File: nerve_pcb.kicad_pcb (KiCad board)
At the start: 6 copper layers, 50 x 50 mm, 72 parts, among them J1 TC2050-IDC, J2 2171750001, J4 472192001, J5 BF030-16A-B1-0360-0277-0600-LB, J6 2x15, J7 CAN1, J8 CAN2, SW1 SPST, SW2 SPST, U1 ld39150dt33-r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

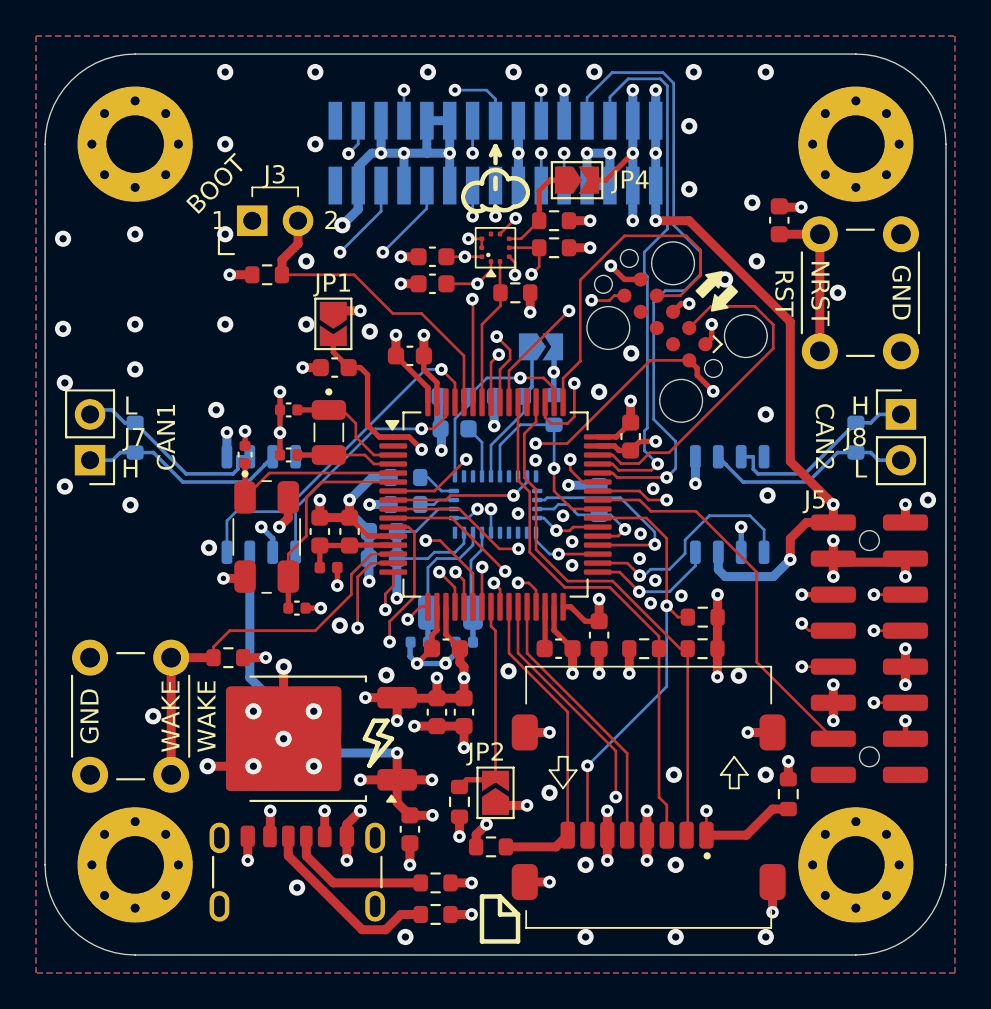
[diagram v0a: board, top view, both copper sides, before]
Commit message: Cleanup and update 2x10 Radio connector
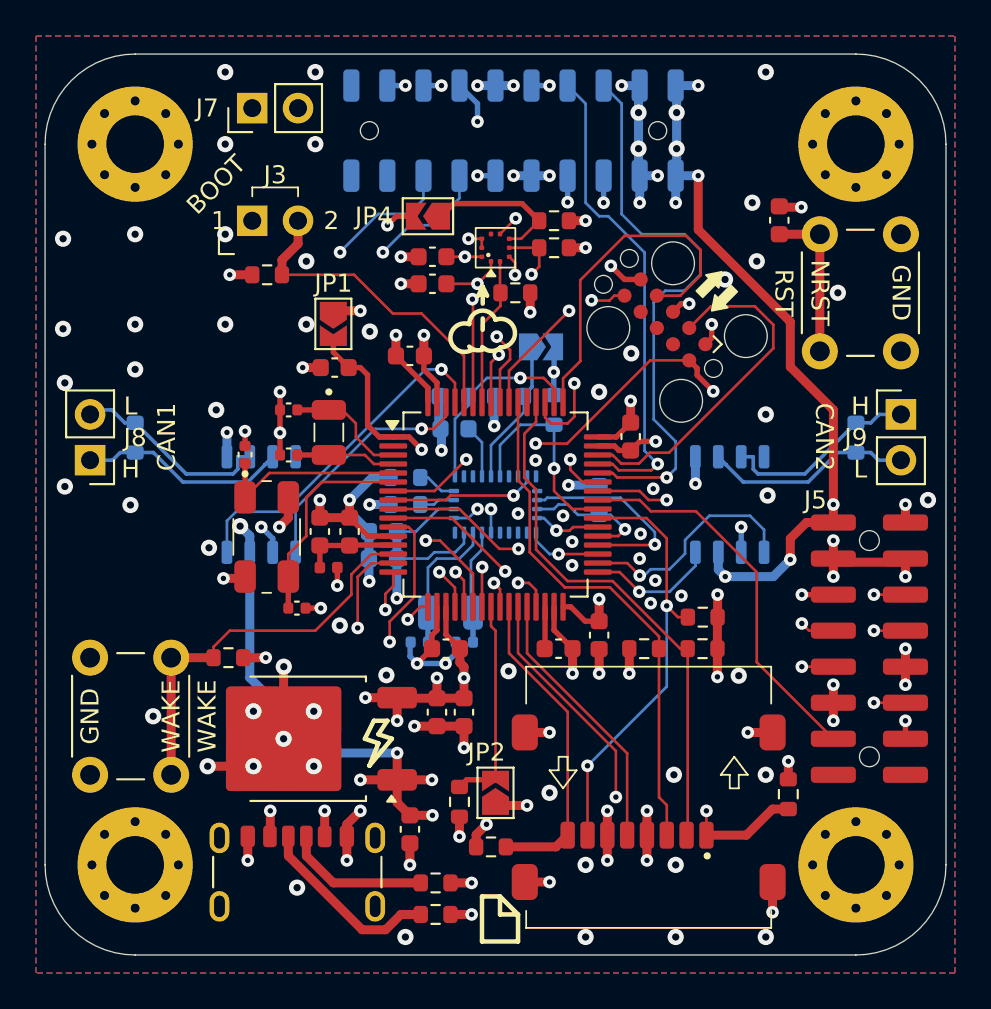
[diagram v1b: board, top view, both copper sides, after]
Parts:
- added J7: UART, Connector_PinHeader_2.54mm:PinHeader_1x02_P2.54mm_Vertical, F.Cu at (135.0, 83.0)
- J6: value 2x15 -> BF080-20-A-1-L-C; footprint Connector_PinSocket_1.27mm:PinSocket_2x15_P1.27mm_Vertical_SMD -> connectors:bf080-20-a-1-l-c
- moved JP4 8.51 mm to (144.8, 89.0), turned to 180 degrees
- moved J6 1.60 mm to (149.5, 84.2), turned to 180 degrees
- renumbered J7 to J8, J8 to J9
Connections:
- J6 pad 10: /USART1_TX -> GND
- J6 pad 11: /GPIO_RADIO_RST -> GND
- J6 pad 12: /USART1_RX -> /PB5
- J6 pad 13: GND -> /PB4
- J6 pad 14: GND -> /PA6
- J6 pad 15: /PA4 -> /PA5
- J6 pad 16: /PB4 -> /PA7
- J6 pad 17: /PA5 -> /PA4
- J6 pad 18: /PB5 -> GND
- J6 pad 19: GND -> unconnected-(J6-Pad19)
- J6 pad 20: GND -> unconnected-(J6-Pad20)
- J6 pad 5: /USART1_RTS -> /USART1_CTS
- J6 pad 6: GND -> /USART1_TX
- J6 pad 7: /USART1_CTS -> /USART1_RTS
- J6 pad 8: GND -> /USART1_RX
- J6 pad 9: GND -> /GPIO_RADIO_RST
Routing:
- net GND: track 129.6 -> 102.6 mm, vias 126 -> 116
- net +5V: track 68.2 -> 77.1 mm, vias 12 -> 16
- net /PB4: track 14.3 -> 20.4 mm
- net /USART1_CTS: track 35.7 -> 31.7 mm
- net /USART1_TX: track 28.0 -> 24.0 mm
- net /USART1_RTS: track 30.7 -> 27.0 mm
- net /USART3_TX: track 41.8 -> 38.5 mm, vias 2 -> 1
- net Net-(JP4-A): track 5.36 -> 8.21 mm
- net /PA7: track 30.4 -> 32.9 mm
- net /PA6: track 27.8 -> 30.1 mm
- net /PA5: track 31.2 -> 33.4 mm
- net /USART1_RX: track 22.5 -> 20.3 mm
- net /PA4: track 36.2 -> 34.0 mm
- net /PB5: track 13.8 -> 15.5 mm
- net /USART3_RX: track 34.1 -> 34.9 mm, vias 2 -> 1
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
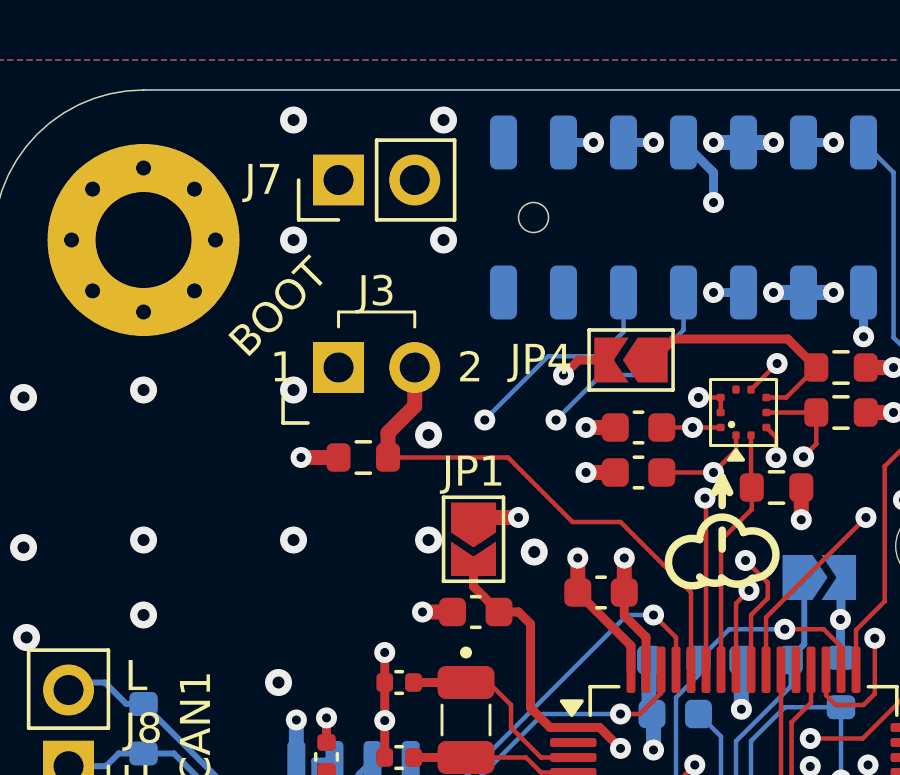
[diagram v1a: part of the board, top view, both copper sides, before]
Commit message: Cleanup schematic and change J7 footprint
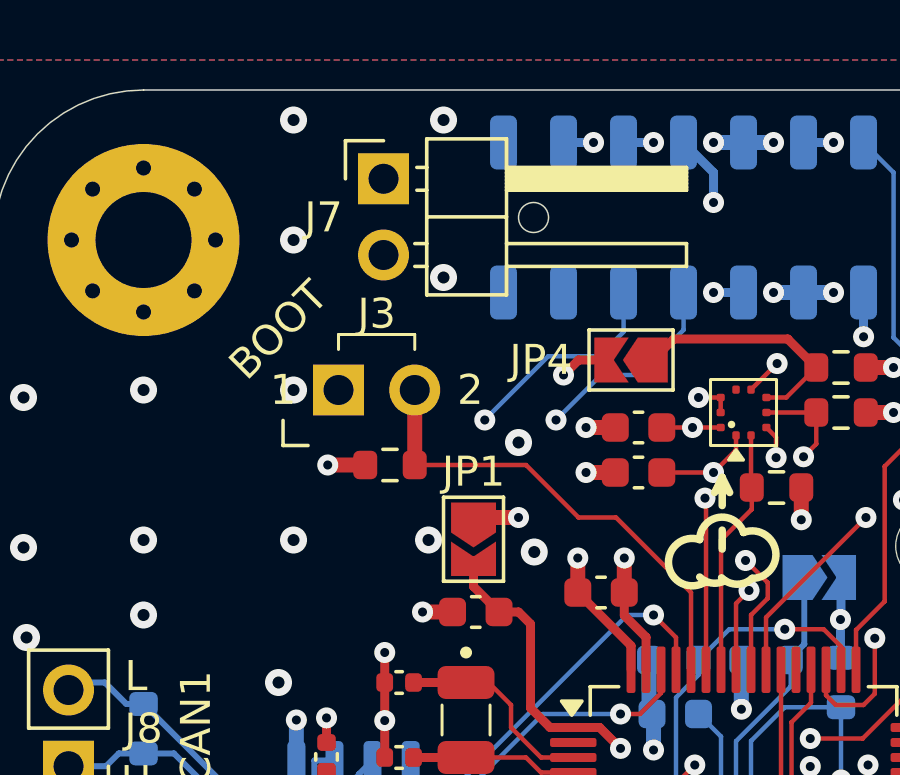
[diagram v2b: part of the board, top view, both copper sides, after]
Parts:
- J7: footprint Connector_PinHeader_2.54mm:PinHeader_1x02_P2.54mm_Vertical -> Connector_PinHeader_2.54mm:PinHeader_1x02_P2.54mm_Horizontal
- moved J7 1.50 mm to (136.5, 83.0), turned to 0 degrees
- moved R9 0.92 mm to (136.7, 92.5)
- moved J3 0.75 mm to (136.3, 90.0)
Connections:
- J7 pad 1: /USART3_TX -> /USART3_RX
- J7 pad 2: /USART3_RX -> /USART3_TX
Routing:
- net /USART3_TX: track 38.5 -> 35.3 mm
- net /BOOT0: track 17.9 -> 16.0 mm

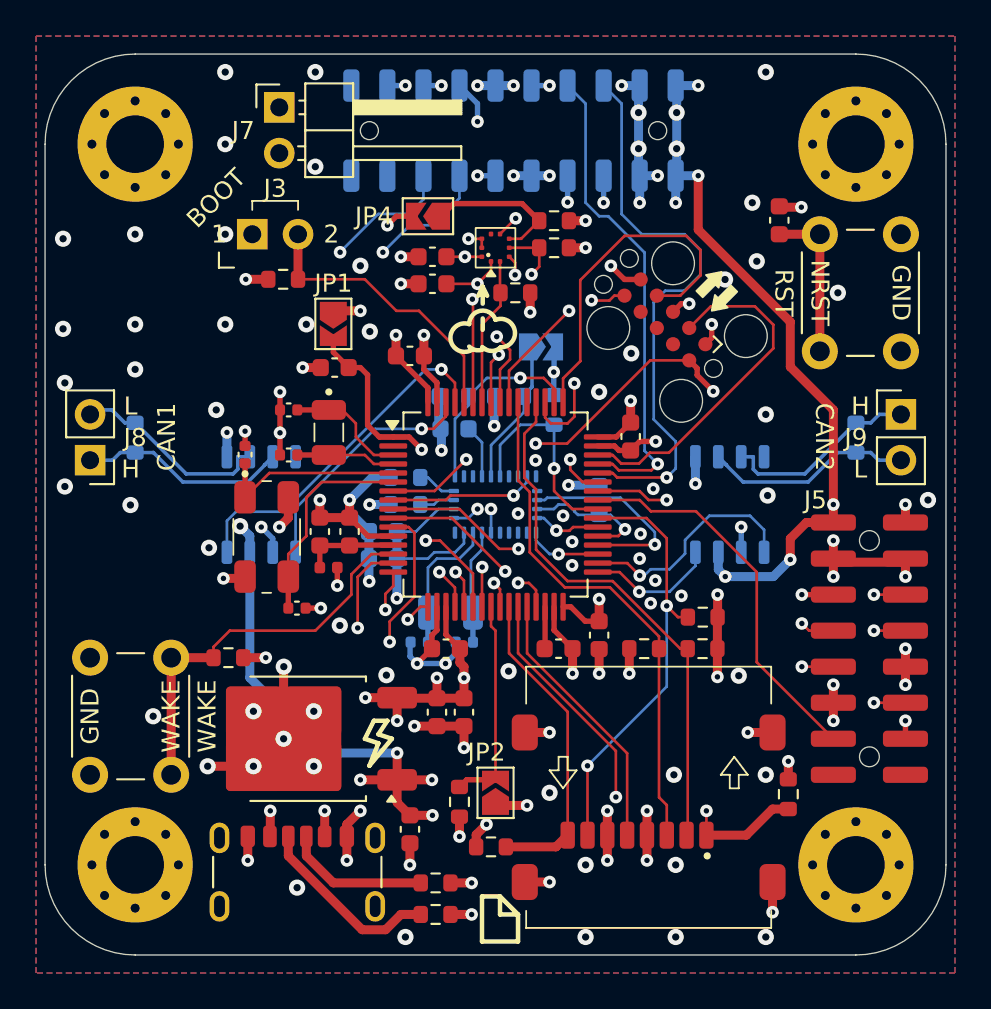
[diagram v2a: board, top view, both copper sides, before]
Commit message: Add WS2812Bs
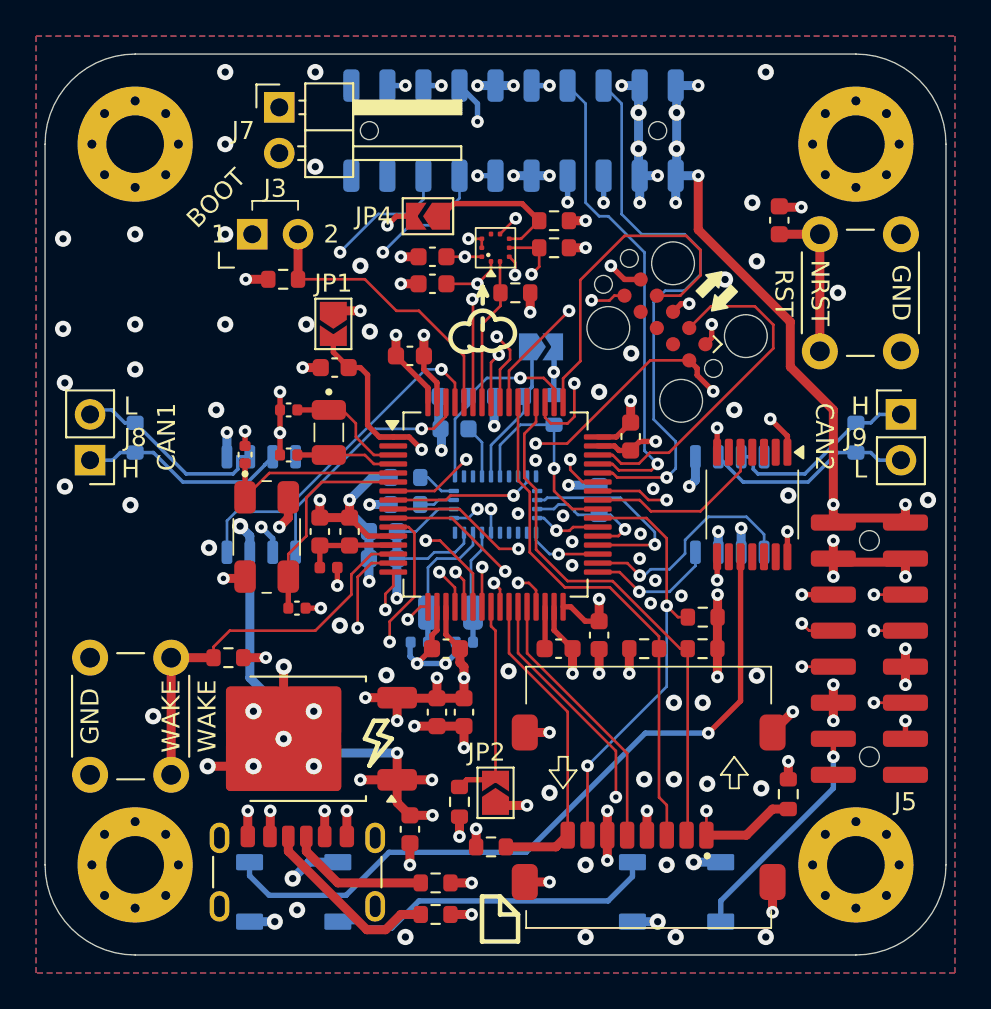
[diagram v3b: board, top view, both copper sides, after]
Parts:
- added D1: WS2812B, LED_SMD:LED_WS2812B_PLCC4_5.0x5.0mm_P3.2mm, B.Cu at (137.3, 126.5)
- added D2: WS2812B, LED_SMD:LED_WS2812B_PLCC4_5.0x5.0mm_P3.2mm, B.Cu at (158.6, 126.5)
- added U3: TXB0104QPWRQ1, common:txb0104qpwrq1, F.Cu at (162.8, 105.0)
- renumbered U3 to U4, U4 to U5, U5 to U6, U6 to U7
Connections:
- J5 pad 14: /TIM1_CH1_PWM -> /WS2812B_PWM
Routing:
- net /TIM1_CH1_PWM_{5V}: track 0.00 -> 40.9 mm, vias 0 -> 1
- net Net-(D1-DOUT): track 0.00 -> 18.5 mm
- net /WS2812B_PWM: track 0.00 -> 12.7 mm, vias 0 -> 1
- net /TIM1_CH1_PWM: track 21.5 -> 10.2 mm
- net GND: track 102.6 -> 105.4 mm, vias 116 -> 122
- net +3V3: track 88.7 -> 90.6 mm, vias 39 -> 40
- net +5V: track 77.1 -> 78.8 mm, vias 16 -> 18

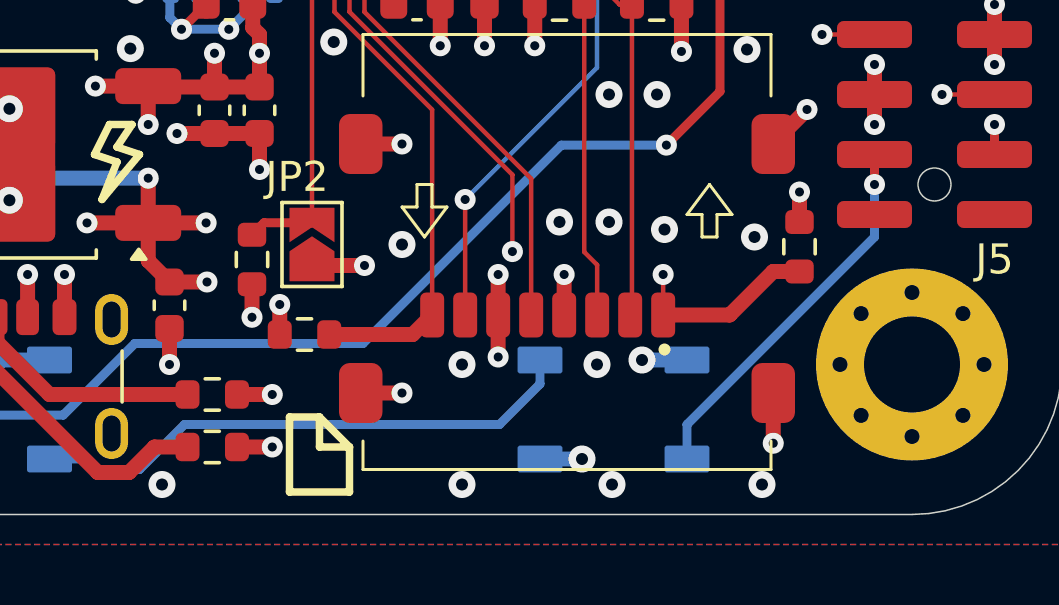
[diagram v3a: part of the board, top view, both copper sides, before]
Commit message: Fix D2 position for symmetry
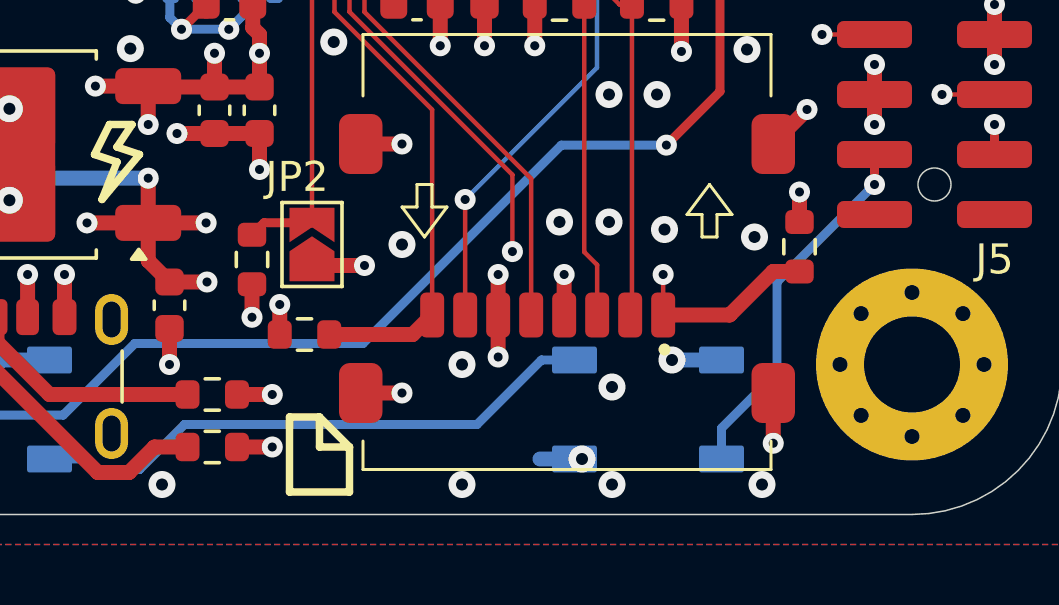
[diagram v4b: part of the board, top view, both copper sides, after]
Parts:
- moved D2 1.15 mm to (159.7, 126.5)
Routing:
- net Net-(D1-DOUT): track 18.5 -> 19.2 mm
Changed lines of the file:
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@@
 	(footprint "LED_SMD:LED_WS2812B_PLCC4_5.0x5.0mm_P3.2mm"
 		(layer "B.Cu")
-		(at 158.55 126.5 180)
+		(at 159.7 126.5 180)
 		(descr "5.0mm x 5.0mm Addressable RGB LED NeoPixel, https://cdn-shop.adafruit.com/datasheets/WS2812B.pdf")
 		(tags "LED RGB NeoPixel PLCC-4 5050")
 		(property "Reference" "D2"
-			(at 0 3.5 360)
+			(at 0 3.5 0)
 			(layer "B.SilkS")
 			(effects
@@
 		)
 		(property "Value" "WS2812B"
-			(at 0 -4 360)
+			(at 0 -4 0)
 			(layer "B.Fab")
 			(effects
@@
 		)
 		(fp_text user "1"
-			(at -4.15 1.6 360)
+			(at -4.15 1.6 0)
 			(layer "B.SilkS")
 			(effects
@@
 		)
 		(fp_text user "${REFERENCE}"
-			(at 0 0 360)
+			(at 0 0 0)
 			(layer "B.Fab")
 			(effects
@@
 	)
 	(via
-		(at 158 125)
+		(at 158.5 125.75)
 		(size 0.9)
 		(drill 0.4)
@@
 	)
 	(via
-		(at 159.5 124.85)
+		(at 160.5 124.85)
 		(size 0.9)
 		(drill 0.4)
@@
 	)
 	(segment
-		(start 159.5 124.85)
-		(end 161 124.85)
-		(width 0.5)
-		(layer "B.Cu")
-		(net 4)
-	)
-	(segment
 		(start 137.243628 125.756372)
 		(end 138.15 124.85)
@@
 	)
 	(segment
+		(start 160.5 124.85)
+		(end 162.15 124.85)
+		(width 0.5)
+		(layer "B.Cu")
+		(net 4)
+	)
+	(segment
 		(start 134.865 106.74)
 		(end 134.865 107.65)
@@
 	)
 	(segment
-		(start 140.873604 128.15)
-		(end 141.223604 128.5)
+		(start 154 127)
+		(end 156.15 124.85)
 		(width 0.3)
 		(layer "B.Cu")
@@
 	)
 	(segment
-		(start 139.75 128.15)
-		(end 140.873604 128.15)
+		(start 142.75 128.5)
+		(end 144.25 127)
 		(width 0.3)
 		(layer "B.Cu")
@@
 	)
 	(segment
-		(start 142.75 128.5)
-		(end 144.25 127)
+		(start 140.873604 128.15)
+		(end 141.223604 128.5)
 		(width 0.3)
 		(layer "B.Cu")
@@
 	)
 	(segment
-		(start 156.1 125.65)
-		(end 156.1 124.85)
+		(start 141.223604 128.5)
+		(end 142.75 128.5)
 		(width 0.3)
 		(layer "B.Cu")
@@
 	)
 	(segment
-		(start 144.25 127)
-		(end 154.75 127)
+		(start 156.15 124.85)
+		(end 157.25 124.85)
 		(width 0.3)
 		(layer "B.Cu")
@@
 	)
 	(segment
-		(start 154.75 127)
-		(end 156.1 125.65)
+		(start 144.25 127)
+		(end 154 127)
 		(width 0.3)
 		(layer "B.Cu")
@@
 	)
 	(segment
-		(start 141.223604 128.5)
-		(end 142.75 128.5)
+		(start 139.75 128.15)
+		(end 140.873604 128.15)
 		(width 0.3)
 		(layer "B.Cu")
@@
 	)
 	(segment
-		(start 161 128.15)
-		(end 161 127)
+		(start 162.15 127.125)
+		(end 164 125.275)
 		(width 0.3)
 		(layer "B.Cu")
@@
 	)
 	(segment
-		(start 167.25 120.75)
+		(start 164 122.25)
 		(end 167.25 119)
 		(width 0.3)
@@
 	)
 	(segment
-		(start 161 127)
-		(end 167.25 120.75)
+		(start 162.15 128.15)
+		(end 162.15 127.125)
+		(width 0.3)
+		(layer "B.Cu")
+		(net 73)
+	)
+	(segment
+		(start 164 125.275)
+		(end 164 122.25)
 		(width 0.3)
 		(layer "B.Cu")

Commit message: Fix via position to prevent USB-C short
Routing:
- net +5V: track 79.0 -> 80.4 mm
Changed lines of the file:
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@@
 	)
 	(via
-		(at 137.243628 125.756372)
+		(at 137.75 122)
 		(size 0.9)
 		(drill 0.4)
@@
 	)
 	(segment
+		(start 137.75 122)
+		(end 137.75 124)
+		(width 0.5)
+		(layer "B.Cu")
+		(net 4)
+	)
+	(segment
+		(start 138.6 124.85)
+		(end 139.75 124.85)
+		(width 0.5)
+		(layer "B.Cu")
+		(net 4)
+	)
+	(segment
+		(start 137.75 124)
+		(end 138.6 124.85)
+		(width 0.5)
+		(layer "B.Cu")
+		(net 4)
+	)
+	(segment
 		(start 158.5 86.75)
 		(end 158.5 88.25)
@@
 	)
 	(segment
-		(start 138.15 124.85)
-		(end 139.75 124.85)
-		(width 0.5)
-		(layer "B.Cu")
-		(net 4)
-	)
-	(segment
 		(start 158.5 86.75)
 		(end 159.75 86.75)
 		(width 0.5)
 		(layer "B.Cu")
-		(net 4)
-	)
-	(segment
-		(start 137.243628 125.756372)
-		(end 138.15 124.85)
-		(width 0.5)
-		(layer "B.Cu")
